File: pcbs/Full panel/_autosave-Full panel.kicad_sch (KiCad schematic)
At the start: 9 parts, among them J1 Conn_01x03_Socket, U1 MAX16832AASA+T

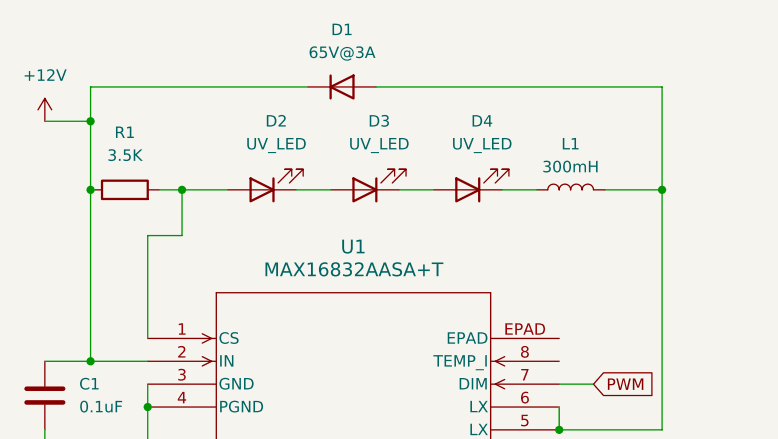
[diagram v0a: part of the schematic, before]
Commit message: full panel with max168
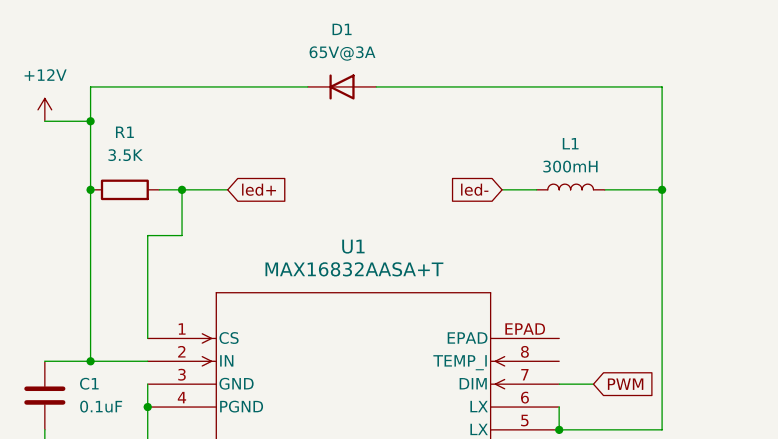
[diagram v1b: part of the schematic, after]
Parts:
- removed D2, D3, D4: UV_LED, symbol Device:LED
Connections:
- net led+: now reaches R1.2, U1.1 (CS)
- net led-: now reaches L1.1
